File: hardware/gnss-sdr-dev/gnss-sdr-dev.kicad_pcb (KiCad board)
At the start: 6 copper layers, 80 x 60 mm, 268 parts, among them J101 CON-SMA-EDGE-S, J401 BM05B-SRSS-TB, J5 USB4110GFA, J501 JTAG, J502 LA, J601 USB4110GFA, U10 ISM6HG256XTR, U101 BGA524N6, U102 BGA855N6, U103 TPS2553DBV, U201 MAX2769B, U202 LMK1C1104PW, U301 MAX2771, U401 ADP7142ARDZ-3.3, U402 LP5907MFX-1.8, U403 TPS62A02APDDC, U404 TLV75725PDBV, U501 LFE5U-25F-6BG256, U502 W25Q128JVSIQ, U6 ESP32-P4NRW32X, U601 USBLC6-2SC6, U7 W25Q128JVYIQ, U8 TLV62569DRLR, U9 TPS62152RGTR, Y1 ECS-400-10-37B2-CKY-TR, Y201 TG2520SMN 27.0000M-MCGNNM3

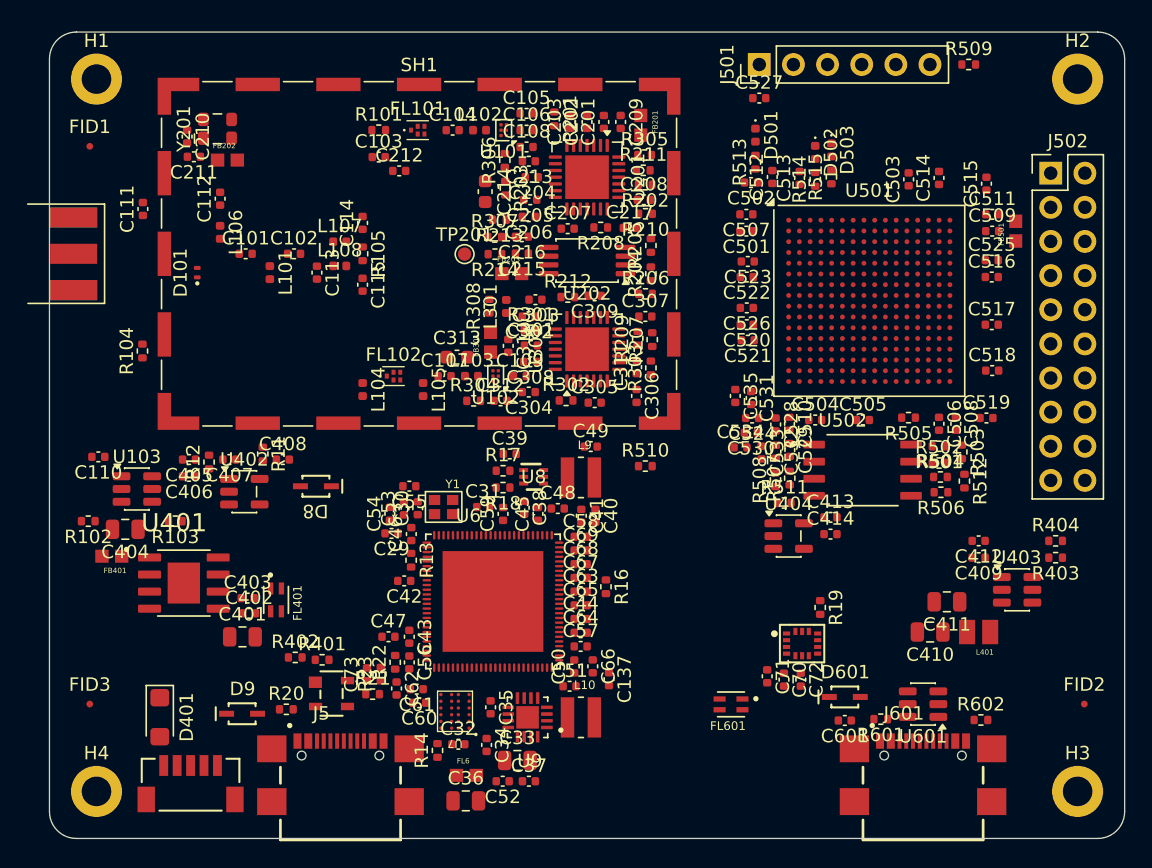
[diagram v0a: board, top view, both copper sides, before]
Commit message: hardware(gnss-sdr-dev): ground planes and the RF section routed -- U201 turned to 0 deg and U301 to 180 deg so both inputs face their chains, receiver passives re-placed per pin, clocks on In2, supply islands on In4
Ground:
- GND In1/In3 planes, GND pours on F.Cu/In2/B.Cu, GND fill on In4 (Space Bug V3 zone settings).
- No pour under the SMA centre pad on F.Cu, In1 or In2, so the pad sees In3 (~55 ohm instead of 11).

RF:
- The SMA hops under the shield wall on In2 (0.13 mm = 50 ohm).
- F.Cu CPWG 0.16/0.2 (50.5 ohm) runs through the bias tee, the divider and both SAW/LNA rows into the receivers.
- The L1 bypass reaches LNA1 by an In2 hop.
- Both LNAOUT -> MIXIN loops are routed; the LNA supplies have ground vias on every ground pin.

Placement (owner-approved):
- U201 at 0 deg, nudged 0.5 mm west and 0.1 mm down. U301 at 180 deg.
- About 60 receiver passives re-placed per pin.
- C105/C108 sit at their own LNAs; U202 is vertical mid-shield.
- Ferrites and bulk caps moved to the empty west side.

Clocks:
- The TCXO line runs on In2, off the RF rows.
- CLKIN, SCLK27_L5 and the REF27 attenuator node run on In2. They are kept off the rows, the L5 match, the L1 loop and U301's exposed-pad via field.

Power:
- +3V3_L1, +3V3_L5 and +3V3_CLK islands on In4 (priority 1).
- +3V3_GNSS and +1V8_LNA come in on In4 from vias in C407/C408.
- +1V8_LNA uses B.Cu for 16 mm to reach U101.

Vias:
- A GND return via beside each signal via where there was room; four sit 1.3-1.7 mm away.
- RF fences, shield-frame stitching and exposed-pad vias.

Left for the owner: the nets leaving the shield end at 20 escape vias.
- SPI and LD/SHDN/IDLE to the P4.
- I/Q and SCLK27_FPGA to the FPGA.
- U103 supply, EN and FLT.

Checks:
- DRC 0 errors. The warnings are the placed board's silkscreen plus the 20 escape vias.
- Schematic parity 0; tools/check_board_parity.py ok (268).

Co-Authored-By: Claude Opus 5.5 <noreply@anthropic.com>
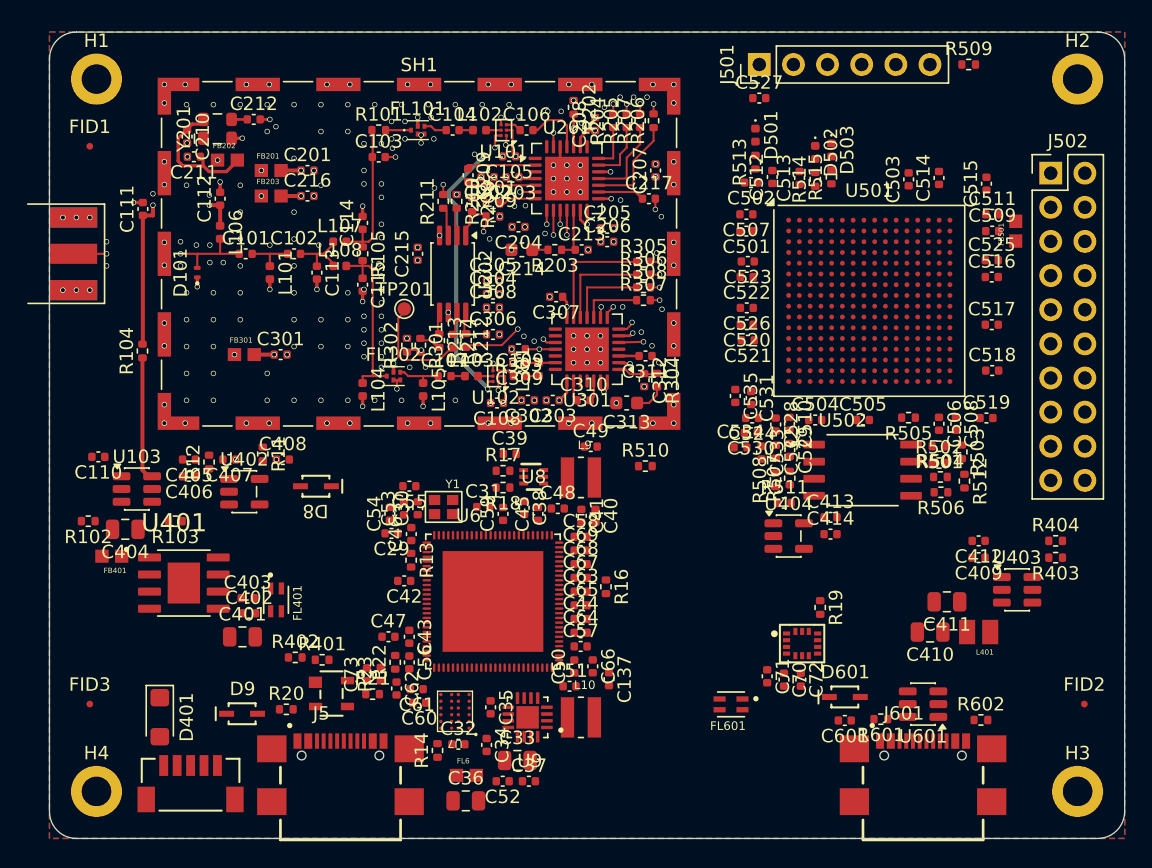
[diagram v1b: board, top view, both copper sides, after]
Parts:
- moved FB201 27.7 mm to (116.5, 110.3), turned to 0 degrees
- moved C201 22.3 mm to (119.2, 110.3), turned to 0 degrees
- moved C108 19.2 mm to (133.3, 127.6), turned to 180 degrees
- moved FB203 18.8 mm to (116.5, 112.2)
- moved C301 18.6 mm to (117.2, 124.0)
- moved FB301 18.3 mm to (114.5, 124.0), turned to 0 degrees
- moved R207 16.3 mm to (143.9, 106.6)
- moved C216 16.2 mm to (119.2, 112.2), turned to 0 degrees
- moved R211 15.1 mm to (129.3, 112.6), turned to 90 degrees
- moved R210 14.1 mm to (130.3, 112.6), turned to -90 degrees
- moved R209 14.1 mm to (133.0, 113.7), turned to 0 degrees
- moved R304 13.7 mm to (145.2, 125.9), turned to -90 degrees
- moved R306 13.4 mm to (144.2, 118.0), turned to 0 degrees
- moved C313 13.1 mm to (142.9, 127.6), turned to 180 degrees
- moved R206 12.9 mm to (144.9, 106.6), turned to 90 degrees
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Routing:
- net +1V8_LNA: track 0.00 -> 50.9 mm, vias 0 -> 6
- net Net-(U201-XTAL): track 0.00 -> 30.2 mm, vias 0 -> 2
- net +3V3_L5: track 0.00 -> 28.3 mm, vias 0 -> 11
- net +3V3_GNSS: track 0.00 -> 25.6 mm, vias 0 -> 5
- net +3V3_L1: track 0.00 -> 24.8 mm, vias 0 -> 13
- net Net-(C311-Pad1): track 0.00 -> 22.8 mm, vias 0 -> 2
- net /RF front end/ANT_BIAS: track 0.00 -> 17.6 mm, vias 0 -> 2
- net Net-(U202-CLKIN): track 0.00 -> 17.6 mm, vias 0 -> 2
- net SCLK27_L5: track 0.00 -> 15.7 mm, vias 0 -> 2
- net GND: track 0.00 -> 14.7 mm, vias 0 -> 238
- net L1_RF_BYP: track 0.00 -> 14.7 mm, vias 0 -> 2
- net /RF front end/ANT: track 0.00 -> 14.5 mm, vias 0 -> 2
- net /RF front end/RF_L5: track 0.00 -> 13.6 mm
- net /RF front end/RF_L1: track 0.00 -> 11.4 mm
- net +3V3_CLK: track 0.00 -> 9.81 mm, vias 0 -> 5
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- added copper zone on In4.Cu, net +3V3_CLK
- added copper zone on In4.Cu, net +3V3_L1
- added copper zone on In4.Cu, net +3V3_L5
- added copper zone on B.Cu, net GND
- added copper zone on F.Cu, net GND
- added copper zone on In1.Cu, net GND
- added copper zone on In2.Cu, net GND
- added copper zone on In3.Cu, net GND
- added copper zone on In4.Cu, net GND

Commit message: hardware(gnss-sdr-dev): the rest of the board routed except the P4's new pins, and the Mantis flight-data NAND added -- FPGA fanout and supplies, sample lines and clock, power entry, IMU, USB-HS connector side; silkscreen references hidden
Silkscreen:
- Reference designators hidden on every part, the new ones included.

Flight-data flash (new sheet "Data flash", flash.kicad_sch):
- U701 is the Mantis U11 part and footprint, GD5F2GQ5UEYIGR (2 Gbit SPI NAND, WSON-8 8x6).
- R701 pulls CS up through reset and boot. R702/R703 pull HOLD#/WP# up, as on the Mantis. C701 is 100 nF.
- It uses the P4's four free GPIOs: GPIO0 = CS, GPIO9 = MISO, GPIO33 = SCK, GPIO34 = MOSI.
  - GPIO34 is the P4's JTAG-source strap, so it only drives the NAND's input and has no pull.
- ERC: 0 errors. The two new warnings are pin-type warnings like those already on the sheet.
- Placed east of the P4 at (147.6, 139). Its locals are routed; its P4 links are not (see below).

Rules:
- New 0.1 mm clearance inside U501's courtyard (0.8 mm BGA), written like the fine-pitch rule for U6/U7/U9/U10.
- Zone fills keep the board default.

Planes:
- +3V3_MCU plane on In4 over the digital side.
- +1V1_FPGA island on B.Cu: the ball field, a finger to each core decoupler, and a strip east of R501-R512 down to the 1.1 V buck.

FPGA:
- Via-in-pad on every supply, ground and interior signal ball.
- Fixed escape lanes run between the ball columns below and south-west of the field.
- Routed:
  - 1.1 V, 2.5 V (on In4, along the east edge) and VCCAUX.
  - The eight sample lines from the shield's escape vias, with their DNP edge-rate shunts.
  - The 27 MHz sample clock out of the shield.
  - Logic-analyzer header (13 of 14 lines), JTAG, status LEDs, config flash and its pull-ups.
  - The CFG_0/1/2 mode straps, on B.Cu under the strap resistors.

Power entry and the west:
- Battery/host connector, input filter, VSS/VSYS/+BATT, VIN to the GNSS LDO and on to the P4 buck's filter.
- GNSS LDO output, +3V3_GNSS and +1V8_LNA, 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
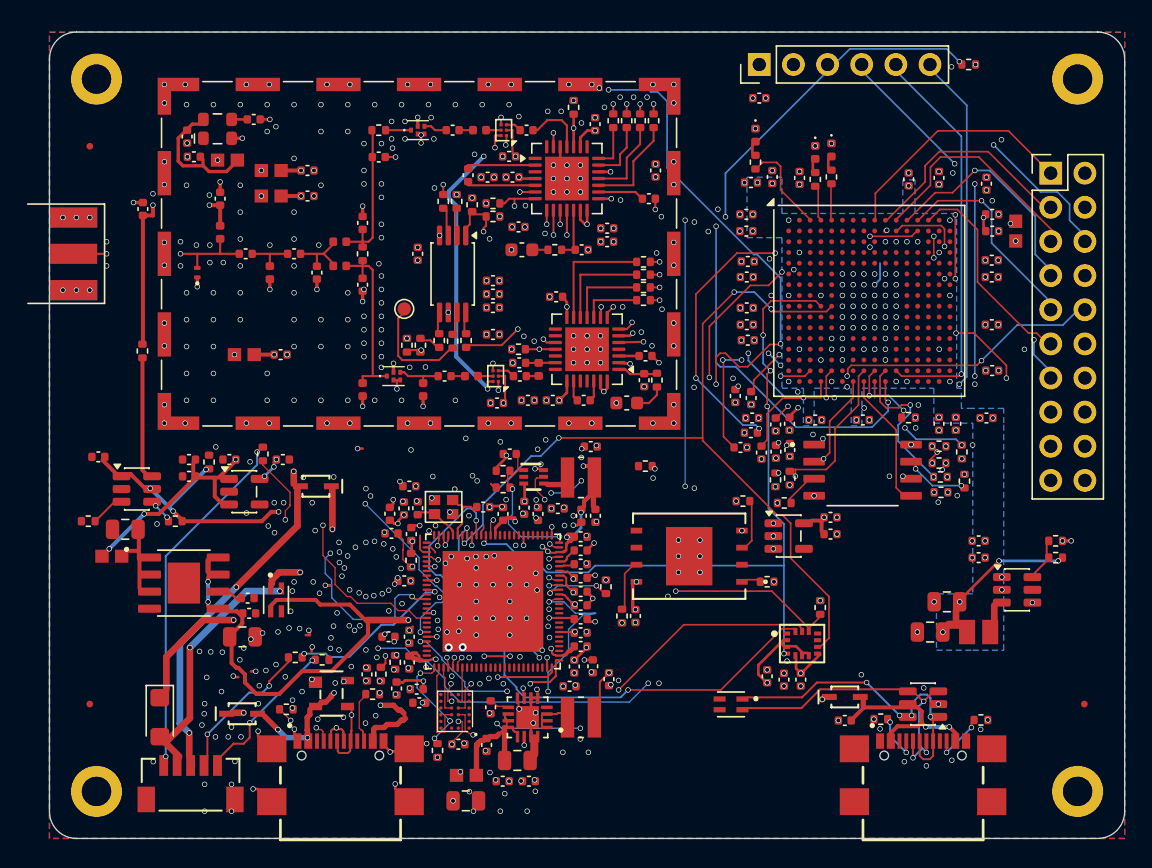
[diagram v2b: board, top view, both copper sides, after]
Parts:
- added C701: 100 nF, Capacitor_SMD:C_0402_1005Metric, F.Cu at (143.6, 143.4)
- added R701: 10 k, Resistor_SMD:R_0402_1005Metric, F.Cu at (153.4, 140.9)
- added R702: 10 k, Resistor_SMD:R_0402_1005Metric, F.Cu at (142.6, 143.4)
- added R703: 10 k, Resistor_SMD:R_0402_1005Metric, F.Cu at (151.6, 134.9)
- added U701: GD5F2GQ5UEYIGR, Footprints:8L_WSON_8x6x3p4x4p3_MAC, F.Cu at (147.6, 139.0)
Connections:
- U6 pad 10: unconnected-(U6A-GPIO9-Pad10) -> NAND_MISO
- U6 pad 104: unconnected-(U6A-GPIO0-Pad104) -> NAND_CS
- U6 pad 64: unconnected-(U6A-GPIO33-Pad64) -> NAND_SCK
- U6 pad 65: unconnected-(U6A-GPIO34-Pad65) -> NAND_MOSI
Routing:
- net L1_LD: track 1.14 -> 108.2 mm, vias 1 -> 7
- net VSYS: track 0.00 -> 79.6 mm, vias 0 -> 6
- net VIN: track 0.00 -> 62.5 mm, vias 0 -> 6
- net ISM6HG256_INT2: track 0.00 -> 62.0 mm, vias 0 -> 4
- net FPGA_CFG_MISO: track 0.00 -> 61.0 mm, vias 0 -> 4
- net ESP_VDD_HP: track 0.00 -> 59.5 mm, vias 0 -> 13
- net L1_I1: track 0.74 -> 59.6 mm, vias 1 -> 5
- net SCLK27_FPGA: track 0.74 -> 58.2 mm, vias 1 -> 4
- net ISM6HG256_INT1: track 0.00 -> 54.9 mm, vias 0 -> 5
- net /FPGA/JTAG_TCK: track 0.00 -> 53.6 mm, vias 0 -> 4
- net L1_I0: track 0.74 -> 52.2 mm, vias 1 -> 6
- net +3V3_MCU: track 0.00 -> 50.4 mm, vias 0 -> 89
- net FE_CS_L5: track 0.79 -> 48.9 mm, vias 1 -> 2
- net L1_Q1: track 0.74 -> 45.8 mm, vias 1 -> 5
- net SENS_SDI: track 0.00 -> 42.8 mm, vias 0 -> 2
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- added copper zone on B.Cu, net +1V1_FPGA
- added copper zone on In4.Cu, net +3V3_MCU
